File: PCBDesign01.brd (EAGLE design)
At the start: 100 x 80 mm, 14 parts, among them IC1 TESEO-LIV3R, U2 VX7805-500

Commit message: more stuff
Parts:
- added C4, C5: (no value), Capacitor:CAPC2012X110
- added D2: CLX6F-FKC-CKNNQDGBB7A363, CLX6F-FKC-CKNNQDGBB7A363:SOJ100P350X290-6N
- added IND, LEDB, LEDG, LEDR, R2: (no value), Resistor:RESC2012X65
- added J1: 5051102491, 5051102491:5051102491
- C1, C2, C3: value C_CHIP-0805(2012-METRIC) -> (none)
- renumbered D1 to PWR-INDICATOR, LS1 to BUZZER
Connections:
- new net N$1: D2.3, LEDR.1
- new net N$2: D2.2, LEDG.1
- new net N$4: D2.1, LEDB.1
- new net N$6: IND.1, PWR-INDICATOR.1
- new net N$7: J1.17, R2.1
- new net N$8: C5.1, J1.14
- new net N$9: C4.1, J1.8
- net GND: now also BUZZER.2, C4.2, C5.2, IND.2, J1.10, J1.23, J1.25, J1.26, LEDB.2, LEDG.2, LEDR.2, R2.2

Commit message: more stuff
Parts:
- added C10: 4.7uF, Capacitor:CAPC2012X110
- added C11: 0.1uF, Capacitor:CAPC2012X110
- added C6, C7, C8, C9: 1uF, Capacitor:CAPC2012X110
- added R10, R11, R12, R13, R8, R9: 0, Resistor:RESC2012X65
- added R4, R6, R7: 10k, Resistor:RESC2012X65
- added R5: 3.3K, Resistor:RESC2012X65
- added U$5: 74LVC07APW, 74LVC07APW:TSSOP-14
- added U$6: ESP-PROG_JTAG_HEADER, ESP-PROG:SAMTEC-FTS-105-01-X-D
- added U$7: ESP-PROG_PROGRAM_HEADER, ESP-PROG:SAMTEC-FTS-103-01-X-D
- added U$8: (no value), Button:BUTTON
- added U1: TPS71913-28DRVR, TPS71913-28DRVR:DRV6_1P6X1
- C1, C2, C5: value (none) -> 0.1uF
- C3: value (none) -> 10nF
- C4: value (none) -> 4.7uF
- LEDB: value (none) -> 200
- LEDG: value (none) -> 230
- LEDR: value (none) -> 193
- R1: value (none) -> 10k
- R2: value (none) -> 3.3K
- R3: value (none) -> 87
- moved R2 104.8 mm to (-260.4, -200.7)
- moved C5 39.4 mm to (-259.1, -144.8)
- moved C4 29.7 mm to (-259.1, -129.5)
- moved U$1 8.13 mm to (-90.2, 11.4)
- renumbered IND to R3
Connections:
- net SCL renamed I2C_SCL
- net SDA renamed I2C_SDA
- net SIN renamed SIG
- net WP renamed N$15
- removed net AD0: U$1.9
- removed net CD: U$3.10
- removed net DAT0: U$3.7
- removed net DAT1: U$3.8
- removed net DAT2: U$3.9
- removed net DAT3: U$3.1
- removed net EXP: A1.39
- removed net FSYNC: U$1.11
- removed net N$7: J1.17, R2.1
- removed net N$8: C5.1, J1.14
- removed net N$9: C4.1, J1.8
- removed net SCK: U$3.5
- new net 1.3V: C9.2, J1.10
- new net 2.8V: C7.1, J1.4, U1.3
- new net 2.8V1: C10.1
- new net 3.3V2: C8.1, U1.1
- new net BUZZER: U$5.9
- new net BUZZER_OUT: BUZZER.1, U$5.8
- new net CAM_I2C_SCL: A1.37, J1.5, R2.2
- new net CAM_I2C_SDA: A1.30, J1.3, R5.2
- new net CAM_PWDN: A1.11, J1.8
- new net CAM_RESET: A1.31, J1.6
- new net CAM_RESET1: R4.1
- new net CAM_RESET2: R6.1
- new net DVP_HREF: A1.12, J1.9
- new net DVP_PCLK: A1.10, J1.17
- new net DVP_VSYNC: A1.29, J1.7
- new net DVP_Y2: A1.6, J1.19
- new net DVP_Y3: J1.21, R9.2
- new net DVP_Y4: J1.22, R8.2
- new net DVP_Y5: A1.7, J1.20
- new net DVP_Y6: A1.5, J1.18
- new net DVP_Y7: J1.16, R10.2
- new net DVP_Y8: A1.24, J1.14
- new net DVP_Y9: A1.4, J1.12
- new net JTAG_TCK: A1.16, R9.1, U$6.4
- new net JTAG_TDI: A1.14, R10.1, U$6.8
- new net JTAG_TDO: A1.23, R11.1, U$6.6
- new net JTAG_TMS: A1.13, R8.1, U$6.2
- new net LEDB_OUT: D2.6, U$5.6
- new net LEDG_OUT: D2.5, U$5.4
- new net LEDR_OUT: D2.4, U$5.2
- new net LED_B: R11.2, U$5.5
- new net LED_G: R13.1, U$5.3
- new net LED_R: R12.1, U$5.1
- new net N$21: A1.1, A1.15, A1.38, A1.39
- new net N$23: U$7.4
- new net N$31: A1.8
- new net N$32: A1.9
- new net PROGRAM_EN: U$7.1
- new net PROGRAM_EN1: A1.3, C11.2, R7.1, U$8.B, U$8.B@1
- new net PROGRAM_IO0: A1.25, U$7.6
- new net PROGRAM_RX: A1.34, R12.2, U$7.5
- new net PROGRAM_TX: A1.35, R13.2, U$7.3
- new net SD_CMD: A1.19, U$3.2
- new net SD_DAT0: A1.21, U$3.7
- new net SD_DAT1: A1.22, U$3.8
- new net SD_DAT2: A1.17, U$3.9
- new net SD_DAT3: A1.18, U$3.1
- new net SD_SCK: A1.20, U$3.5
- new net XMCLK: A1.26, J1.13
- net 3.3V: now also C4.1, C5.1, C6.1, IC1.6, J1.11, PWR-INDICATOR.2, R2.1, R5.1, R6.2, R7.2, U$6.1, U$7.2, U1.2, U1.4, U1.6
- net 5V: now also U$5.14
- net GND: now also C10.2, C11.1, C6.2, C7.2, C8.2, C9.1, J1.15, J1.2, R4.2, U$1.11, U$1.9, U$5.7, U$6.3, U$6.5, U$6.7, U$6.9, U$8.A, U$8.A@1, U1.5, U1.7; no longer A1.1, A1.15, A1.38, IC1.10, J1.10, J1.23, R2.2, U$4.3
- net N$5: now also IC1.10, U$4.3; no longer U$3.2

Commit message: moar
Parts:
- removed R1: 10k, Resistor:RESC2012X65
- removed R12, R13: 0, Resistor:RESC2012X65
- added BACK-LEFT, BACK-RIGHT, FRONT-LEFT, FRONT-RIGHT: ESC, ESC:MA03-1
- added R15: 10k, Resistor:RESC2012X65
- added U$10, U$11, U$12, U$13, U$14, U$15, U$16, U$17, U$18, U$19, U$20, U$21, U$22, U$23, U$24, U$25, U$26, U$27, U$9: TESTPOINT, Test Point:TESTPOINT
- added U3: CD40109BPWR, CD40109BPWR:SOP65P640X120-16N
- added U4: FXL6408UMX, FXL6408UMX:QFN40P260X180X55-16N
- U$8: value (none) -> RESET
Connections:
- removed net 2.8V1: C10.1
- removed net 3.3V2: C8.1, U1.1
- removed net CAM_RESET1: R4.1
- removed net CAM_RESET2: R6.1
- removed net N$15: R1.2, U$3.11
- removed net N$31: A1.8
- removed net N$32: A1.9
- removed net PROGRAM_EN1: A1.3, C11.2, R7.1, U$8.B, U$8.B@1
- new net ESCL_BL: U3.9
- new net ESC_BL_OUT: U$25.0, U3.11
- new net ESC_BR: U3.15
- new net ESC_BR_OUT: U$27.0, U3.13
- new net ESC_FL: U3.7
- new net ESC_FL_OUT: FRONT-LEFT.3, U$26.0, U3.5
- new net ESC_FR: U3.2
- new net ESC_FR_OUT: FRONT-RIGHT.3, U$24.0, U3.4
- new net GPS_RX: A1.8, IC1.3, U$11.0
- new net GPS_TX: A1.9, IC1.2, U$12.0
- new net N$18: R11.2
- new net N$27: U4.6
- new net SD_CD: U$3.10, U4.4
- new net SD_WP: U$3.11, U4.3
- net 1.3V: now also C8.1, U$17.0, U1.1
- net 2.8V: now also C10.1, U$18.0
- net 3.3V: now also R15.2, U$15.0, U3.1, U4.15, U4.2
- net 5V: now also BACK-LEFT.2, BACK-RIGHT.2, FRONT-LEFT.2, FRONT-RIGHT.2, U$16.0, U3.10, U3.14, U3.16, U3.3, U3.6
- net BUZZER: now also U4.7
- net CAM_PWDN: now also R4.1
- net CAM_RESET: now also R6.1
- net GND: now also A1.1, A1.15, A1.38, A1.39, BACK-LEFT.1, BACK-RIGHT.1, FRONT-LEFT.1, FRONT-RIGHT.1, U$14.0, U$19.0, U$20.0, U$21.0, U$22.0, U$7.4, U3.8, U4.16, U4.9; no longer R1.1
- net I2C_SCL: now also U$10.0, U4.13; no longer IC1.17
- net I2C_SDA: now also U$9.0, U4.14; no longer IC1.16
- net LED_B: now also U4.8; no longer R11.2
- net LED_G: now also U4.11; no longer R13.1
- net LED_R: now also U4.12; no longer R12.1
- net N$21: now also U4.5; no longer A1.1, A1.15, A1.38, A1.39
- net N$23: now also R15.1, U4.10; no longer U$7.4
- net PROGRAM_EN: now also A1.3, C11.2, R7.1, U$23.0, U$8.B, U$8.B@1
- net PROGRAM_RX: no longer R12.2
- net PROGRAM_TX: no longer R13.2
- net VBAT: now also U$13.0
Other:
- board size 100 x 80 mm -> 101.6 x 88.9 mm

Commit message: minor resistor changes
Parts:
- LEDG: value 230 -> 226
- LEDR: value 193 -> 200
- R3: value 87 -> 86.6
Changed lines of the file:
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@@
 <attribute name="VALUE" x="-242.57" y="-65.84" size="1.27" layer="27" align="center"/>
 </element>
-<element name="LEDR" library="Resistor" library_urn="urn:adsk.eagle:library:16378527" package="RESC2012X65" package3d_urn="urn:adsk.eagle:package:16378559/2" value="193" x="-248.92" y="-73.66" smashed="yes">
+<element name="LEDR" library="Resistor" library_urn="urn:adsk.eagle:library:16378527" package="RESC2012X65" package3d_urn="urn:adsk.eagle:package:16378559/2" value="200" x="-248.92" y="-73.66" smashed="yes">
 <attribute name="CATEGORY" value="Resistor" x="-248.92" y="-73.66" size="1.778" layer="27" display="off"/>
 <attribute name="MANUFACTURER" value="" x="-248.92" y="-73.66" size="1.778" layer="27" display="off"/>
@@
 <attribute name="VALUE" x="-248.92" y="-75.3191" size="1.27" layer="27" align="top-center"/>
 </element>
-<element name="LEDG" library="Resistor" library_urn="urn:adsk.eagle:library:16378527" package="RESC2012X65" package3d_urn="urn:adsk.eagle:package:16378559/2" value="230" x="-248.92" y="-78.74" smashed="yes">
+<element name="LEDG" library="Resistor" library_urn="urn:adsk.eagle:library:16378527" package="RESC2012X65" package3d_urn="urn:adsk.eagle:package:16378559/2" value="226" x="-248.92" y="-78.74" smashed="yes">
 <attribute name="CATEGORY" value="Resistor" x="-248.92" y="-78.74" size="1.778" layer="27" display="off"/>
 <attribute name="MANUFACTURER" value="" x="-248.92" y="-78.74" size="1.778" layer="27" display="off"/>
@@
 <attribute name="VALUE" x="-248.92" y="-85.4791" size="1.27" layer="27" align="top-center"/>
 </element>
-<element name="R3" library="Resistor" library_urn="urn:adsk.eagle:library:16378527" package="RESC2012X65" package3d_urn="urn:adsk.eagle:package:16378559/2" value="87" x="-248.92" y="-91.44" smashed="yes">
+<element name="R3" library="Resistor" library_urn="urn:adsk.eagle:library:16378527" package="RESC2012X65" package3d_urn="urn:adsk.eagle:package:16378559/2" value="86.6" x="-248.92" y="-91.44" smashed="yes">
 <attribute name="CATEGORY" value="Resistor" x="-248.92" y="-91.44" size="1.778" layer="27" display="off"/>
 <attribute name="MANUFACTURER" value="" x="-248.92" y="-91.44" size="1.778" layer="27" display="off"/>

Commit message: pressure sensor
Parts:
- added C12, C13, C14, C15, C16: 10uF, Capacitor:CAPC2012X110
- added C17, C18, C19, C20, C21: 0.1uF, Capacitor:CAPC2012X110
- added R1: 1k, Resistor:RESC2012X65
- added R12, R13, R18, R19, R20, R21: 10k, Resistor:RESC2012X65
- added R14, R16, R17: 0, Resistor:RESC2012X65
- C3: value 10nF -> 0.1uF
- U$5: value 74LVC07APW -> SPL06-007; device 74LVC07APW:TSSOP-14 -> SPL06-007:SPL06-007
- U4: value FXL6408UMX -> MCP23017T-E/SO; device FXL6408UMX:QFN40P260X180X55-16N -> MCP23017T-E_SO:SOIC127P1030X265-28N
- moved U$5 891.0 mm to (-346.0, -992.0)
- moved R15 841.7 mm to (-330.2, 330.2)
- moved C6 802.9 mm to (-279.4, -965.2)
- moved U4 510.5 mm to (-330.2, -990.6)
- moved U2 35.9 mm to (-64.8, -17.8)
- moved PS1 26.8 mm to (-76.1, -6.92)
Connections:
- removed net BUZZER_OUT: BUZZER.1, U$5.8
- removed net ESCL_BL: U3.9
- removed net LEDB_OUT: D2.6, U$5.6
- removed net LEDG_OUT: D2.5, U$5.4
- removed net LEDR_OUT: D2.4, U$5.2
- removed net N$21: U4.5
- removed net N$27: U4.6
- removed net SD_SCK: A1.20, U$3.5
- new net ESC_BL: U3.9, U4.3
- new net N$19: R20.1, U4.16
- new net N$20: R19.1, U4.15
- new net SD_CLK: R8.2, U$3.5
- net 3.3V: now also C15.2, C16.2, C17.2, C19.2, C20.2, C21.2, R12.1, R13.1, R18.1, U$5.6, U$5.8, U4.9; no longer U4.15, U4.2
- net 5V: now also C14.2, C18.2; no longer U$5.14
- net BUZZER: now also BUZZER.1, R1.1, U4.24; no longer U$5.9, U4.7
- net CAM_PWDN: now also U4.6; no longer A1.11
- net CAM_RESET: now also U4.5; no longer A1.31
- net DVP_Y3: now also R14.2; no longer R9.2
- net DVP_Y4: now also R17.1; no longer R8.2
- net DVP_Y7: now also R16.1; no longer R10.2
- net DVP_Y8: now also A1.31; no longer A1.24
- net ESC_BR: now also U4.4
- net ESC_FL: now also U4.2
- net ESC_FR: now also U4.1
- net GND: now also C12.1, C13.1, C14.1, C15.1, C16.1, C17.1, C18.1, C19.1, C20.1, C21.1, R1.2, R19.2, R20.2, R21.2, U$5.1, U4.10; no longer U4.16, U4.9
- net I2C_SCL: now also U$5.4, U4.12; no longer U4.13
- net I2C_SDA: now also R18.2, U$5.3, U4.13; no longer U4.14
- net LED_B: now also D2.6, U4.23; no longer U$5.5, U4.8
- net LED_G: now also D2.5, U4.22; no longer U$5.3, U4.11
- net LED_R: now also D2.4, U4.21; no longer U$5.1, U4.12
- net N$18: now also R21.1, U4.17; no longer R11.2
- net N$23: now also U4.18; no longer U4.10
- net PROGRAM_IO0: now also R14.1
- net PROGRAM_RX: now also R17.2
- net PROGRAM_TX: now also R16.2
- net SD_CD: now also U4.26; no longer U4.4
- net SD_CMD: now also R11.2, R12.2; no longer A1.19
- net SD_DAT0: now also A1.24, R13.2; no longer A1.21
- net SD_DAT1: now also A1.26; no longer A1.22
- net SD_DAT2: now also R10.2; no longer A1.17
- net SD_DAT3: now also R9.2; no longer A1.18
- net SD_WP: now also U4.25; no longer U4.3
- net VBAT: now also C12.2, C13.2
- net XMCLK: now also A1.11; no longer A1.26
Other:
- board outline removed

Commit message: doing pcb layout
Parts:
- removed R19, R20, R21: 10k, Resistor:RESC2012X65
- removed U$2: LARGE_BATTERY, CustomBattery:LARGE_BATTERY
- removed U2: VX7805-500, VX7805-500:VX78012-500_VX7805-500
- added C22: 47pF, C0402C470K5GACTU:CAPC1005X55N
- added C23: 0.1uF, Capacitor:CAPC2012X110
- added L1: 39nH, 0402 Inductor:IND0402_22N_TAI_TAY-M
- added U$28: AS78L05RTR-E1, AS78L05RTR-E1:VREG_AP2204RA-3.3TRG1
- added U$29: LARGE_BATTERY, CustomBattery:LARGE_BATTERY
- LEDB: value 200 -> 30
- LEDG: value 226 -> 60
- LEDR: value 200 -> 80
- moved U4 1074.1 mm to (-13.4, 35.7), turned to 90 degrees
- moved C6 1047.8 mm to (-43.2, 55.6), flipped to the bottom, turned to 90 degrees
- moved R1 1043.8 mm to (12.1, 18.7), flipped to the bottom, turned to 90 degrees
- moved U$5 1027.3 mm to (-38.0, -12.0)
- moved C15 1014.2 mm to (-33.4, 50.1), flipped to the bottom, turned to 90 degrees
- moved C14 995.0 mm to (-17.0, 52.0), flipped to the bottom, turned to 90 degrees
- moved C13 965.8 mm to (-28.0, 50.0), flipped to the bottom, turned to 90 degrees
- moved C12 944.8 mm to (-21.0, 52.0), flipped to the bottom, turned to 90 degrees
- moved U$9 818.2 mm to (-8.40, -66.2)
- moved U$10 807.1 mm to (-9.00, -69.2)
- moved U$26 790.5 mm to (-1.40, -72.8)
- moved U$27 779.2 mm to (-1.00, -75.8)
- moved U$24 772.7 mm to (-1.40, -66.4)
- moved U$25 761.3 mm to (-1.00, -69.4)
- moved U$23 751.7 mm to (4.60, -66.0)
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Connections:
- removed net N$18: R21.1, U4.17
- removed net N$19: R20.1, U4.16
- removed net N$20: R19.1, U4.15
- removed net N$5: IC1.10, U$4.3
- removed net SIG: IC1.11, U$4.2
- new net ANT: C22.2, L1.2, U$4.2
- new net N$21: C22.1, IC1.11
- new net VCC_RF: C23.2, IC1.14, L1.1
- net 3.3V: now also U3.15, U3.2, U3.7, U3.9
- net 5V: now also U$28.1; no longer U2.3, U3.10, U3.14, U3.3, U3.6
- net ESC_BL: now also U3.10; no longer U3.9
- net ESC_BL_OUT: now also BACK-LEFT.3
- net ESC_BR: now also U3.14; no longer U3.15
- net ESC_BR_OUT: now also BACK-RIGHT.3
- net ESC_FL: now also U3.6; no longer U3.7
- net ESC_FR: now also U3.3; no longer U3.2
- net GND: now also C23.1, IC1.10, U$28.2, U$29.GND, U$4.3, U4.15, U4.16, U4.17; no longer R19.2, R20.2, R21.2, U$2.GND, U2.2
- net VBAT: now also U$28.3, U$29.V_BAT; no longer U$2.V_BAT, U2.1
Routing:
- net 3.3V: track 0.00 -> 23.5 mm
- net 1.3V: track 0.00 -> 11.2 mm
- net VBAT: track 0.00 -> 7.84 mm, vias 0 -> 1
- net 5V: track 0.00 -> 6.43 mm, vias 0 -> 1
- net N$6: track 0.00 -> 5.06 mm
- net 2.8V: track 0.00 -> 4.86 mm
- net N$1: track 0.00 -> 4.33 mm
- net N$4: track 0.00 -> 4.24 mm
- net N$2: track 0.00 -> 3.47 mm
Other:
- board outline added: 101.6 x 101.6 mm

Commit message: ready for pcb review
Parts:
- removed U$14, U$19, U$20, U$22: TESTPOINT, Test Point:TESTPOINT
- LEDG: value 60 -> 60.4
- LEDR: value 80 -> 80.6
- R3: value 86.6 -> 80.6
- moved U$27 132.6 mm to (41.0, 50.0), turned to 180 degrees
- moved U$21 130.5 mm to (-44.4, 44.0)
- moved U$26 124.3 mm to (41.0, 44.0), turned to 180 degrees
- moved U$25 123.7 mm to (41.0, 47.0), turned to 180 degrees
- moved C1 122.0 mm to (5.98, 12.9), flipped to the bottom
- moved U$23 119.2 mm to (-41.4, 44.0)
- moved U$24 115.5 mm to (41.0, 41.0), turned to 180 degrees
- moved C23 113.2 mm to (14.0, -17.5), flipped to the bottom
- moved U$17 111.9 mm to (-44.4, 41.0)
- moved C3 108.5 mm to (3.31, 12.9), flipped to the bottom
- moved U$18 106.0 mm to (-44.4, 38.0)
- moved C2 105.4 mm to (1.00, 24.8), flipped to the bottom, turned to 270 degrees
- moved U$13 104.0 mm to (-44.4, 29.0)
- moved U$15 103.4 mm to (-44.4, 35.0)
- moved U$16 103.2 mm to (-44.4, 32.0)
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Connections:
- net GND: now also A1.P$1, U$1.25, U$1.P$1; no longer U$14.0, U$19.0, U$20.0, U$22.0
- net LED_B: now also U4.21; no longer U4.23
- net LED_R: now also U4.23; no longer U4.21
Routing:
- net 5V: track 6.43 -> 309.1 mm, vias 1 -> 5
- net ESC_FL_OUT: track 0.00 -> 216.1 mm
- net GND: track 0.00 -> 146.8 mm, vias 0 -> 59
- net I2C_SCL: track 0.00 -> 135.7 mm, vias 0 -> 3
- net PROGRAM_EN: track 0.00 -> 128.4 mm, vias 0 -> 5
- net I2C_SDA: track 0.00 -> 128.1 mm, vias 0 -> 4
- net ESC_FR_OUT: track 0.00 -> 126.8 mm, vias 0 -> 1
- net ESC_BL_OUT: track 0.00 -> 125.3 mm
- net 3.3V: track 23.5 -> 140.4 mm, vias 0 -> 31
- net SD_DAT0: track 0.00 -> 111.3 mm, vias 0 -> 1
- net SD_DAT1: track 0.00 -> 105.7 mm, vias 0 -> 1
- net BUZZER: track 0.00 -> 87.8 mm, vias 0 -> 2
- net CAM_I2C_SCL: track 0.00 -> 85.9 mm, vias 0 -> 7
- net SD_CD: track 0.00 -> 84.2 mm, vias 0 -> 2
- net PROGRAM_IO0: track 0.00 -> 82.3 mm, vias 0 -> 3
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- added copper zone on layer 1, net 3.3V
- added copper zone on layer 16, net GND
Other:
- board text added: "1.3V"
- board text added: "2.8V"
- board text added: "3.3V"
- board text added: "5V"
- board text added: ">"
- board text added: "BL"
- board text added: "BR"
- board text added: "ENABLE"
- board text added: "ESC"
- board text added: "FL"
- board text added: "FR"
- board text added: "GND"
- board text added: "GPS"
- board text added: "I2C"
- board text added: "RX"
- board text added: "SCL"
- board text added: "SDA"
- board text added: "TX"
- board text added: "VBAT"

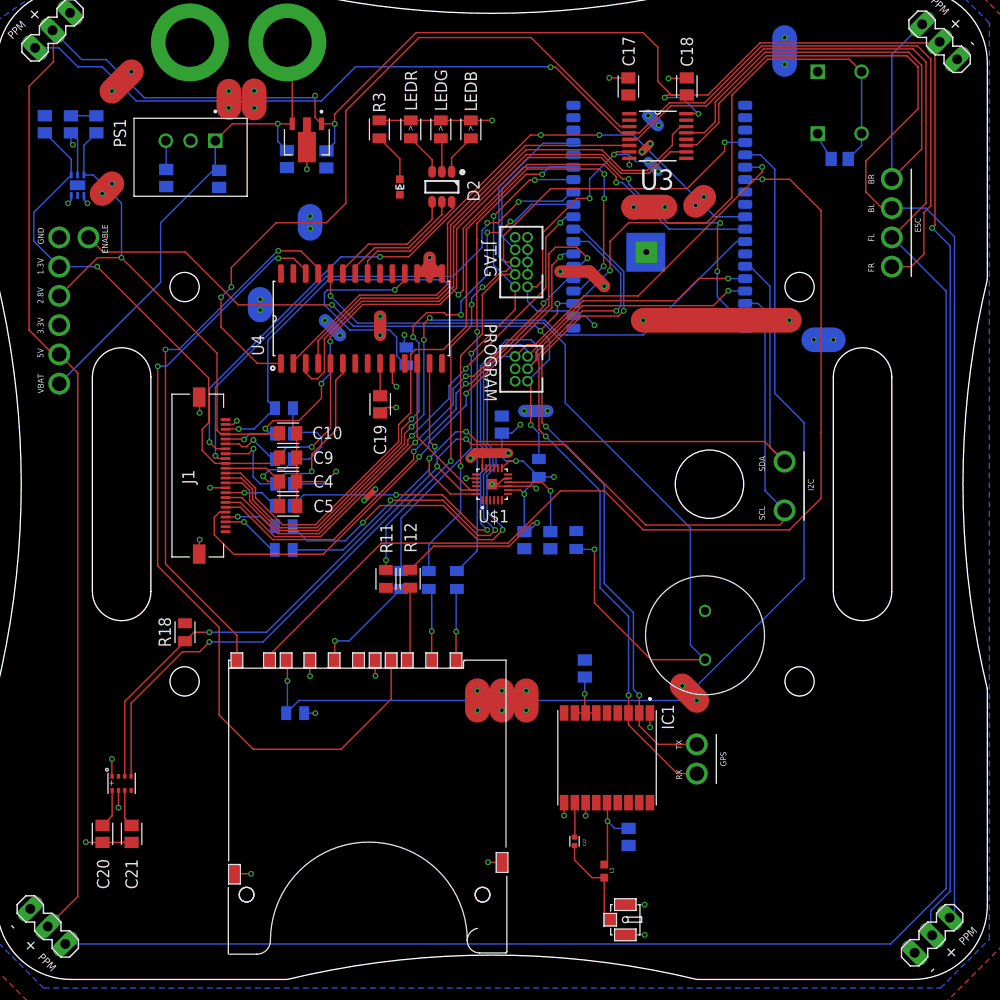
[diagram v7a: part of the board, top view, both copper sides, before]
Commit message: add magnetometer
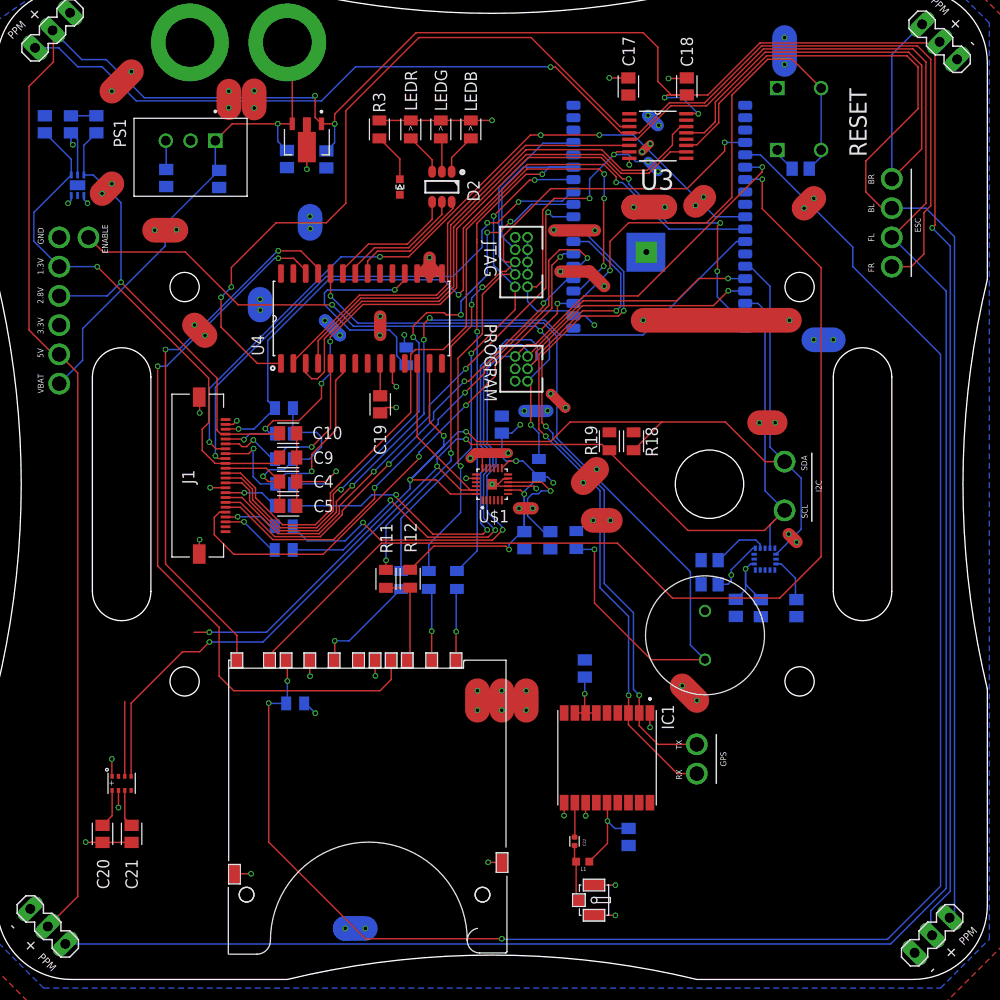
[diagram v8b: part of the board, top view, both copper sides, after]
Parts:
- added C24, C25, C26, C27: 0.1uF, Capacitor:CAPC2012X110
- added C28: 4.7uF, Capacitor:CAPC2012X110
- added R19: 10k, Resistor:RESC2012X65
- added U2: FXOS8700CQR1, FXOS8700CQR1 Magnetometer:QFN16_3X3_NXP
- moved R18 50.0 mm to (14.5, 23.1)
- moved U$8 4.48 mm to (31.8, 56.8)
- moved C11 4.12 mm to (31.7, 51.0)
- moved U$4 3.79 mm to (11.0, -24.0)
- moved L1 2.41 mm to (9.29, -20.0), turned to 180 degrees
- moved R13 1.00 mm to (-20.2, -3.80)
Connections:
- new net N$18: C25.1, U2.2
- new net N$5: C26.1, U2.8
- net 3.3V: now also C24.2, C27.1, C28.1, R19.1, U2.1, U2.14
- net GND: now also C24.1, C25.2, C26.2, C27.2, C28.2, U2.10, U2.12, U2.13, U2.16, U2.3, U2.5, U2.7
- net I2C_SCL: now also R19.2, U2.4
- net I2C_SDA: now also U2.6
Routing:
- net SD_DAT0: track 111.3 -> 181.0 mm, vias 1 -> 3
- net 3.3V: track 140.4 -> 159.9 mm, vias 31 -> 35
- net GND: track 146.8 -> 164.7 mm, vias 59 -> 77
- net I2C_SDA: track 128.1 -> 139.0 mm
- net SD_CD: track 84.2 -> 75.7 mm
- net N$18: track 0.00 -> 5.75 mm
- net N$5: track 0.00 -> 4.84 mm
- net I2C_SCL: track 135.7 -> 140.2 mm
- net PROGRAM_EN: track 128.4 -> 124.2 mm
- net ANT: track 9.86 -> 5.79 mm
- net N$3: track 8.91 -> 12.2 mm
- net SD_DAT1: track 105.7 -> 108.9 mm
- net DVP_PCLK: track 54.9 -> 56.6 mm
- net PROGRAM_IO0: track 82.3 -> 80.9 mm
- net 2.8V: track 51.9 -> 50.8 mm
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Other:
- board text added: "RESET"
